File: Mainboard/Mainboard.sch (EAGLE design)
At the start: 58 parts, among them IC1 TL072CD, IC2 LM386M-1_NOPB, J1 USB3076, J2 640455-5, J3 640455-3, J4 640455-4, J5 640455-4, J6 SJ-3523-SMT-TR, J7 640455-2, J8 929850-01-06-RB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

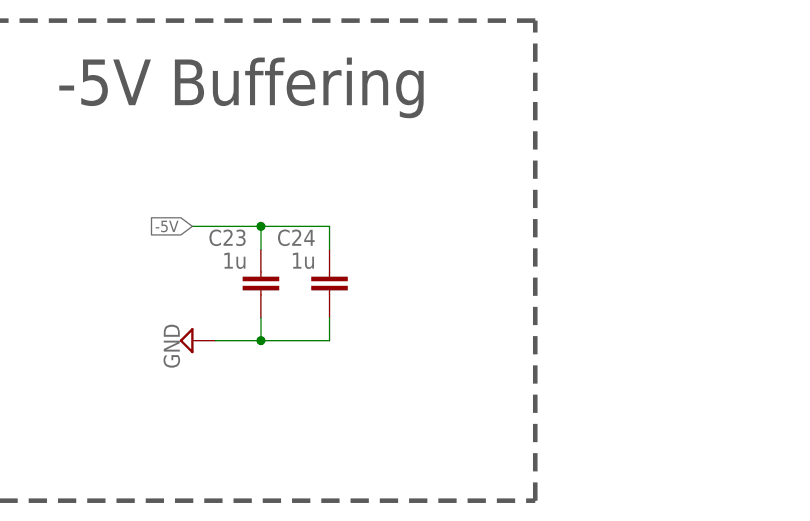
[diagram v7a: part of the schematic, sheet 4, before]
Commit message: Mainboard updated VIII: routed completely, only need to check SD Card size
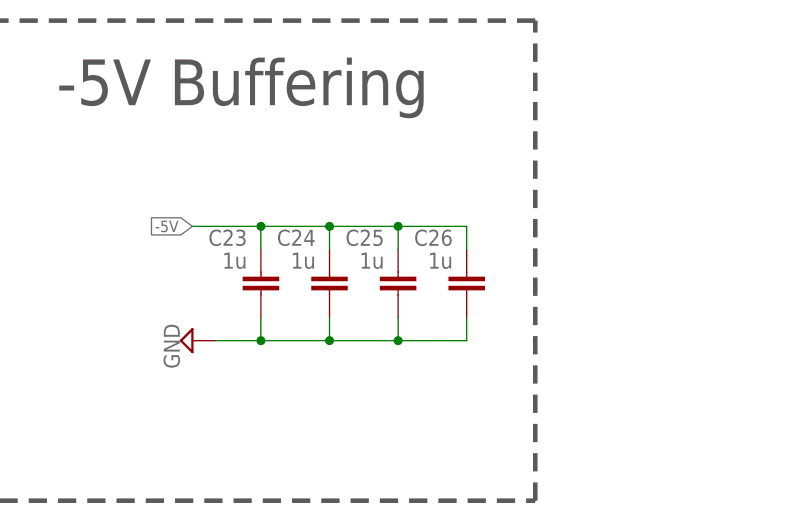
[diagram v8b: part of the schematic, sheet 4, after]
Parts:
- added C25, C26: 1u, rcl:C-EUC0603
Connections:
- net -5V: now also C25.2, C26.2
- net GND: now also C25.1, C26.1
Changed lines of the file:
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@@
 <part name="C24" library="rcl" deviceset="C-EU" device="C0603" value="1u"/>
 <part name="SUPPLY37" library="supply2" deviceset="GND" device=""/>
+<part name="C25" library="rcl" deviceset="C-EU" device="C0603" value="1u"/>
+<part name="C26" library="rcl" deviceset="C-EU" device="C0603" value="1u"/>
 </parts>
 <sheets>
@@
 </instance>
 <instance part="SUPPLY37" gate="GND" x="63.5" y="-68.58" rot="R270"/>
+<instance part="C25" gate="G$1" x="86.36" y="-63.5" smashed="yes" rot="R180">
+<attribute name="NAME" x="84.836" y="-56.261" size="1.778" layer="95" rot="R180"/>
+<attribute name="VALUE" x="84.836" y="-58.801" size="1.778" layer="96" rot="R180"/>
+</instance>
+<instance part="C26" gate="G$1" x="93.98" y="-63.5" smashed="yes" rot="R180">
+<attribute name="NAME" x="92.456" y="-56.261" size="1.778" layer="95" rot="R180"/>
+<attribute name="VALUE" x="92.456" y="-58.801" size="1.778" layer="96" rot="R180"/>
+</instance>
 </instances>
 <busses>
@@
 <junction x="71.12" y="-68.58"/>
 <pinref part="SUPPLY37" gate="GND" pin="GND"/>
+<pinref part="C26" gate="G$1" pin="1"/>
+<wire x1="93.98" y1="-66.04" x2="93.98" y2="-68.58" width="0.1524" layer="91"/>
+<wire x1="93.98" y1="-68.58" x2="86.36" y2="-68.58" width="0.1524" layer="91"/>
+<junction x="78.74" y="-68.58"/>
+<pinref part="C25" gate="G$1" pin="1"/>
+<wire x1="86.36" y1="-68.58" x2="78.74" y2="-68.58" width="0.1524" layer="91"/>
+<wire x1="86.36" y1="-66.04" x2="86.36" y2="-68.58" width="0.1524" layer="91"/>
+<junction x="86.36" y="-68.58"/>
 </segment>
 </net>
@@
 <junction x="71.12" y="-55.88"/>
 <label x="63.5" y="-55.88" size="1.27" layer="95" rot="R180" xref="yes"/>
-</segment>
-</net>
+<wire x1="78.74" y1="-55.88" x2="86.36" y2="-55.88" width="0.1524" layer="91"/>
+<junction x="78.74" y="-55.88"/>
+<pinref part="C26" gate="G$1" pin="2"/>
+<wire x1="86.36" y1="-55.88" x2="93.98" y2="-55.88" width="0.1524" layer="91"/>
+<wire x1="93.98" y1="-55.88" x2="93.98" y2="-58.42" width="0.1524" layer="91"/>
+<pinref part="C25" gate="G$1" pin="2"/>
+<wire x1="86.36" y1="-58.42" x2="86.36" y2="-55.88" width="0.1524" layer="91"/>
+<junction x="86.36" y="-55.88"/>
+</segment>
+</net>
